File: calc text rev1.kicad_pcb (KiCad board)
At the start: 4 copper layers, 65 x 97.8 mm, 9 parts, among them J1 Conn_ARM_SWD_TagConnect_TC203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

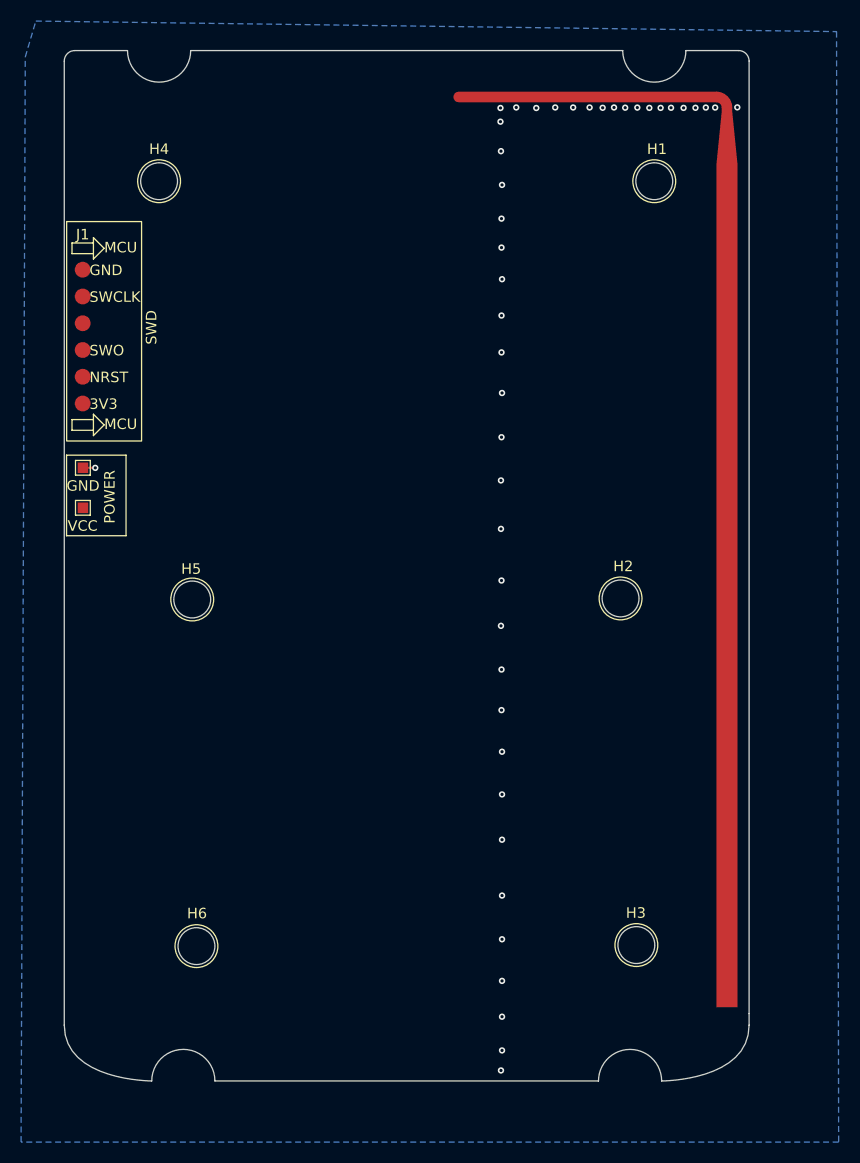
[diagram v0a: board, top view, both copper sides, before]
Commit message: feat: fillet edges + good holes
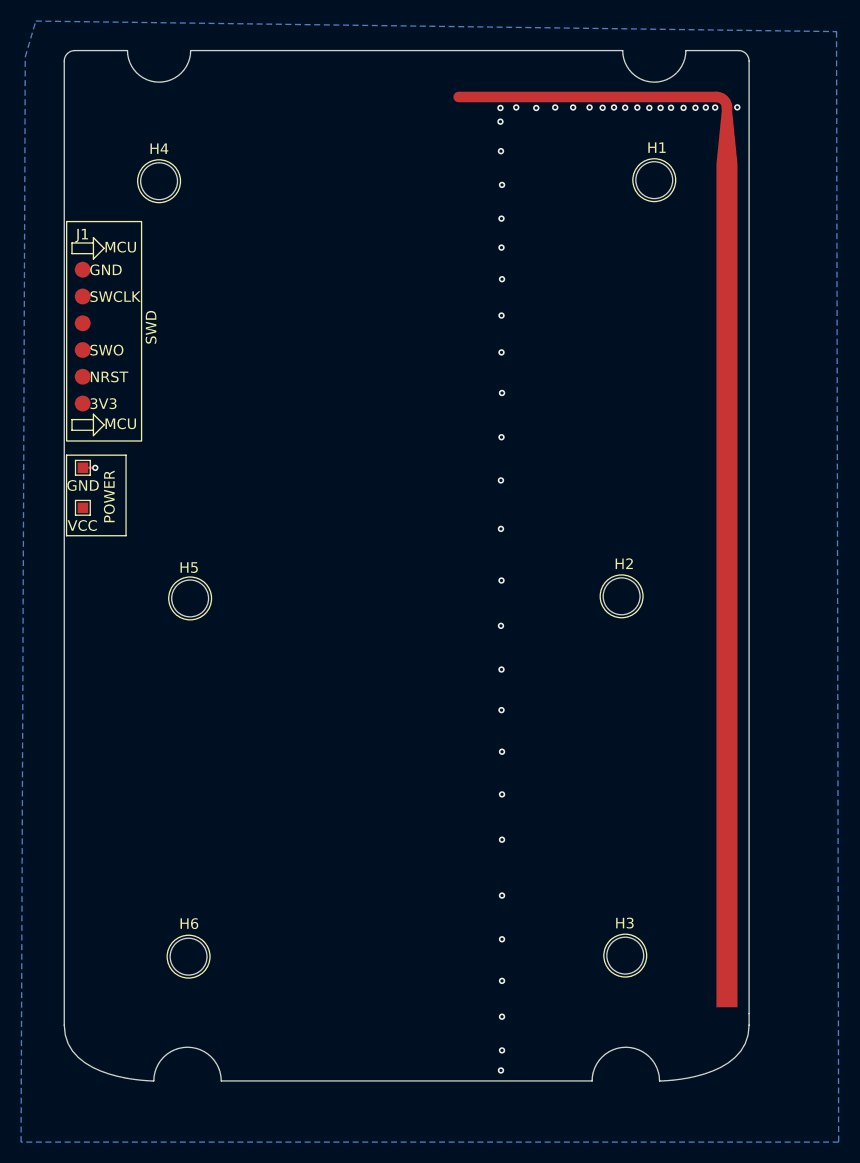
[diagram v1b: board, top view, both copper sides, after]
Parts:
- moved H3 1.45 mm to (70.4, 102.7)
- moved H6 1.25 mm to (29.0, 102.8)
- moved H2 0.22 mm to (70.1, 68.6)
- moved H5 0.22 mm to (29.1, 68.8)
- moved H1 0.10 mm to (73.2, 29.1)
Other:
- outline, holes or cut-outs redrawn
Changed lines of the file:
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@@
 	(footprint "MountingHole:MountingHole_3.5mm_CustomFilled"
 		(layer "F.Cu")
-		(at 69.954 68.8)
+		(at 70.054 68.6)
 		(descr "Mounting Hole 2.1mm, no annular, generated by kicad-footprint-generator mountinghole.py")
 		(tags "mountinghole")
@@
 	(footprint "MountingHole:MountingHole_3.5mm_CustomFilled"
 		(layer "F.Cu")
-		(at 73.154 29.2)
+		(at 73.154 29.1)
 		(descr "Mounting Hole 2.1mm, no annular, generated by kicad-footprint-generator mountinghole.py")
 		(tags "mountinghole")
@@
 	(footprint "MountingHole:MountingHole_3.5mm_CustomFilled"
 		(layer "F.Cu")
-		(at 71.454 101.7)
+		(at 70.4 102.7)
 		(descr "Mounting Hole 2.1mm, no annular, generated by kicad-footprint-generator mountinghole.py")
 		(tags "mountinghole")
@@
 	(footprint "MountingHole:MountingHole_3.5mm_CustomFilled"
 		(layer "F.Cu")
-		(at 29.3 68.9)
+		(at 29.1 68.8)
 		(descr "Mounting Hole 2.1mm, no annular, generated by kicad-footprint-generator mountinghole.py")
 		(tags "mountinghole")
@@
 	(footprint "MountingHole:MountingHole_3.5mm_CustomFilled"
 		(layer "F.Cu")
-		(at 29.7 101.8)
+		(at 28.954 102.8)
 		(descr "Mounting Hole 2.1mm, no annular, generated by kicad-footprint-generator mountinghole.py")
 		(tags "mountinghole")
@@
 		(layer "Edge.Cuts")
 	)
-	(gr_arc
-		(start 25.202538 114.597462)
-		(mid 28.2 111.6)
-		(end 31.197462 114.597462)
-		(stroke
-			(width 0.0381)
-			(type default)
-		)
-		(layer "Edge.Cuts")
-	)
 	(gr_line
 		(start 16.9 17.8)
 		(end 16.9 109.3)
+		(stroke
+			(width 0.0381)
+			(type default)
+		)
+		(layer "Edge.Cuts")
+	)
+	(gr_arc
+		(start 16.9 17.8)
+		(mid 17.192893 17.092893)
+		(end 17.9 16.8)
+		(stroke
+			(width 0.0381)
+			(type default)
+		)
+		(layer "Edge.Cuts")
+	)
+	(gr_arc
+		(start 25.4 114.597462)
+		(mid 28.6 111.397462)
+		(end 31.8 114.597462)
 		(stroke
 			(width 0.0381)
@@
 		(layer "Edge.Cuts")
 	)
-	(gr_line
-		(start 67.605076 114.6)
-		(end 31.197462 114.597462)
-		(stroke
-			(width 0.0381)
-			(type default)
-		)
-		(layer "Edge.Cuts")
-	)
 	(gr_arc
 		(start 28.897462 16.8)
@@
 	)
 	(gr_arc
-		(start 67.605076 114.6)
-		(mid 70.602538 111.602538)
-		(end 73.6 114.6)
-		(stroke
-			(width 0.0381)
-			(type default)
-		)
-		(layer "Edge.Cuts")
-	)
-	(gr_arc
-		(start 16.9 17.8)
-		(mid 17.192893 17.092893)
-		(end 17.9 16.8)
+		(start 80.9 16.8)
+		(mid 81.607107 17.092893)
+		(end 81.9 17.8)
 		(stroke
 			(width 0.0381)
@@
 	(gr_curve
 		(pts
-			(xy 16.9 109.3) (xy 16.9 114.6) (xy 25.202538 114.597462) (xy 25.202538 114.597462)
-		)
+			(xy 16.9 109.3) (xy 16.9 114.6) (xy 25.4 114.597462) (xy 25.4 114.597462)
+		)
+		(stroke
+			(width 0.0381)
+			(type default)
+		)
+		(layer "Edge.Cuts")
+	)
+	(gr_arc
+		(start 67 114.6)
+		(mid 70.2 111.4)
+		(end 73.4 114.6)
+		(stroke
+			(width 0.0381)
+			(type default)
+		)
+		(layer "Edge.Cuts")
+	)
+	(gr_line
+		(start 67 114.6)
+		(end 31.8 114.597462)
 		(stroke
 			(width 0.0381)
@@
 	(gr_curve
 		(pts
-			(xy 81.9 109.3) (xy 81.9 114.6) (xy 73.6 114.6) (xy 73.6 114.6)
-		)
-		(stroke
-			(width 0.0381)
-			(type default)
-		)
-		(layer "Edge.Cuts")
-	)
-	(gr_arc
-		(start 80.9 16.8)
-		(mid 81.607107 17.092893)
-		(end 81.9 17.8)
+			(xy 81.9 109.3) (xy 81.9 114.6) (xy 73.4 114.6) (xy 73.4 114.6)
+		)
 		(stroke
 			(width 0.0381)
@@
 		)
 	)
+	(dimension
+		(type orthogonal)
+		(layer "F.Fab")
+		(pts
+			(xy 28.402538 111.397462) (xy 28.402538 104.8)
+		)
+		(height -3.102538)
+		(orientation 1)
+		(format
+			(prefix "")
+			(suffix "")
+			(units 3)
+			(units_format 0)
+			(precision 4)
+			(suppress_zeroes yes)
+		)
+		(style
+			(thickness 0.1)
+			(arrow_length 1.27)
+			(text_position_mode 0)
+			(arrow_direction outward)
+			(extension_height 0.58642)
+			(extension_offset 0.5)
+			(keep_text_aligned yes)
+		)
+		(gr_text "6.5975"
+			(at 24.15 108.098731 90)
+			(layer "F.Fab")
+			(effects
+				(font
+					(size 1 1)
+					(thickness 0.15)
+				)
+			)
+		)
+	)
+	(dimension
+		(type orthogonal)
+		(layer "F.Fab")
+		(pts
+			(xy 70.4 111.4) (xy 70.4 104.8)
+		)
+		(height 2.7)
+		(orientation 1)
+		(format
+			(prefix "")
+			(suffix "")
+			(units 3)
+			(units_format 0)
+			(precision 4)
+			(suppress_zeroes yes)
+		)
+		(style
+			(thickness 0.1)
+			(arrow_length 1.27)
+			(text_position_mode 0)
+			(arrow_direction outward)
+			(extension_height 0.58642)
+			(extension_offset 0.5)
+			(keep_text_aligned yes)
+		)
+		(gr_text "6.6"
+			(at 71.95 108.1 90)
+			(layer "F.Fab")
+			(effects
+				(font
+					(size 1 1)
+					(thickness 0.15)
+				)
+			)
+		)
+	)

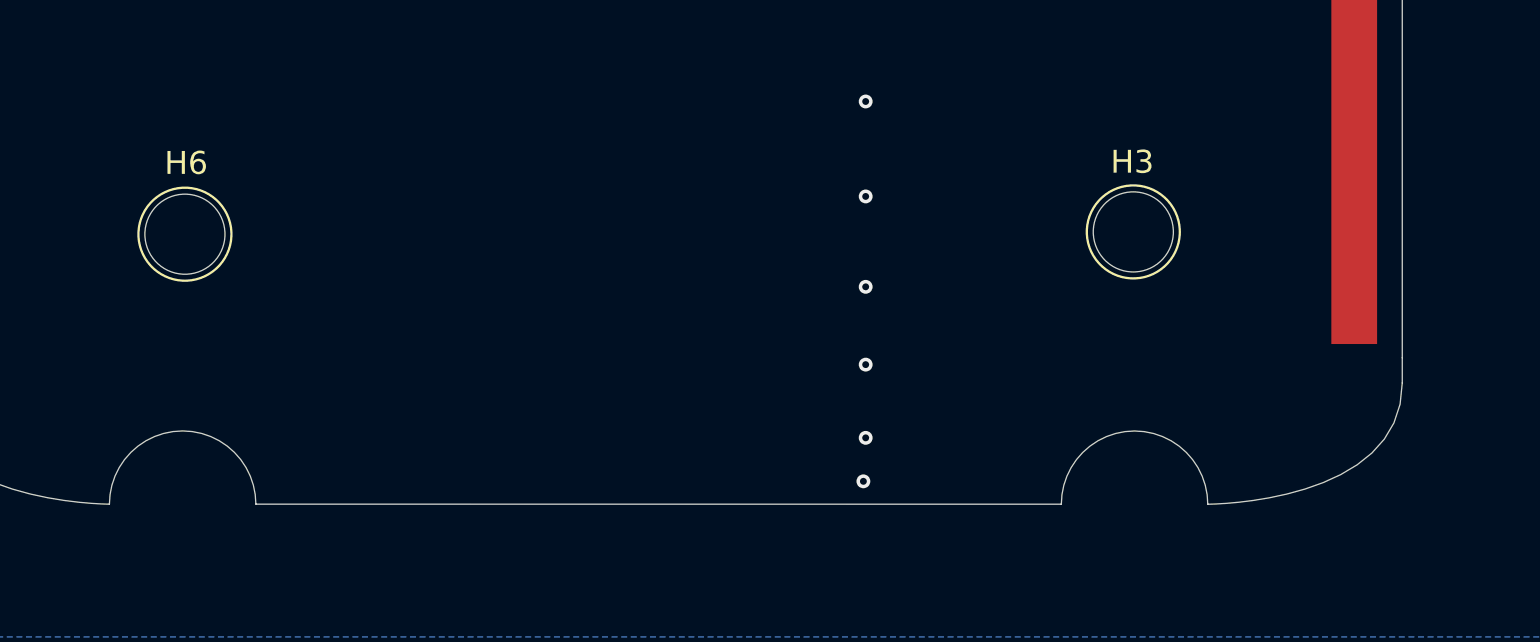
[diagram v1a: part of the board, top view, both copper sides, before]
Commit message: fix: adjust bottom two holes
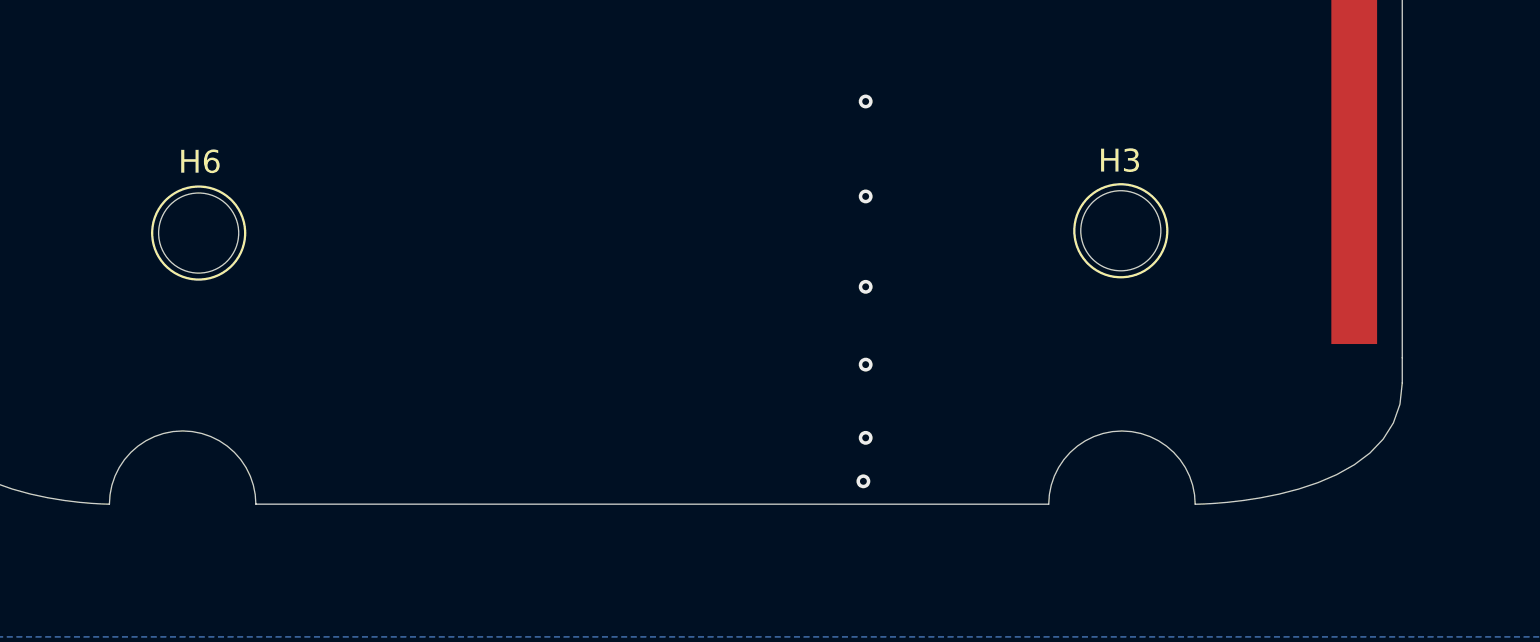
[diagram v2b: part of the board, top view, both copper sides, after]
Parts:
- moved H6 0.60 mm to (29.6, 102.8)
- moved H3 0.55 mm to (69.9, 102.7)
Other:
- outline, holes or cut-outs redrawn
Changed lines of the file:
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@@
 			(outputformat 3)
 			(mirror no)
-			(drillshape 2)
+			(drillshape 1)
 			(scaleselection 1)
 			(outputdirectory "dxf/")
@@
 	(footprint "MountingHole:MountingHole_3.5mm_CustomFilled"
 		(layer "F.Cu")
-		(at 70.4 102.7)
+		(at 69.854 102.65)
 		(descr "Mounting Hole 2.1mm, no annular, generated by kicad-footprint-generator mountinghole.py")
 		(tags "mountinghole")
@@
 	(footprint "MountingHole:MountingHole_3.5mm_CustomFilled"
 		(layer "F.Cu")
-		(at 28.954 102.8)
+		(at 29.554 102.75)
 		(descr "Mounting Hole 2.1mm, no annular, generated by kicad-footprint-generator mountinghole.py")
 		(tags "mountinghole")
@@
 		(layer "Edge.Cuts")
 	)
+	(gr_curve
+		(pts
+			(xy 81.9 109.3) (xy 81.9 114.6) (xy 72.85 114.6) (xy 72.85 114.6)
+		)
+		(stroke
+			(width 0.0381)
+			(type default)
+		)
+		(layer "Edge.Cuts")
+	)
 	(gr_line
 		(start 16.9 17.8)
@@
 		(layer "Edge.Cuts")
 	)
+	(gr_line
+		(start 66.45 114.6)
+		(end 31.8 114.597462)
+		(stroke
+			(width 0.0381)
+			(type default)
+		)
+		(layer "Edge.Cuts")
+	)
 	(gr_arc
 		(start 25.4 114.597462)
@@
 	)
 	(gr_arc
-		(start 67 114.6)
-		(mid 70.2 111.4)
-		(end 73.4 114.6)
-		(stroke
-			(width 0.0381)
-			(type default)
-		)
-		(layer "Edge.Cuts")
-	)
-	(gr_line
-		(start 67 114.6)
-		(end 31.8 114.597462)
-		(stroke
-			(width 0.0381)
-			(type default)
-		)
-		(layer "Edge.Cuts")
-	)
-	(gr_curve
-		(pts
-			(xy 81.9 109.3) (xy 81.9 114.6) (xy 73.4 114.6) (xy 73.4 114.6)
-		)
+		(start 66.45 114.6)
+		(mid 69.65 111.4)
+		(end 72.85 114.6)
 		(stroke
 			(width 0.0381)
@@
 		(layer "F.Fab")
 		(pts
+			(xy 16.9 104.15) (xy 29.2 104)
+		)
+		(height -6.95)
+		(orientation 0)
+		(format
+			(prefix "")
+			(suffix "")
+			(units 3)
+			(units_format 0)
+			(precision 4)
+			(suppress_zeroes yes)
+		)
+		(style
+			(thickness 0.1)
+			(arrow_length 1.27)
+			(text_position_mode 0)
+			(arrow_direction outward)
+			(extension_height 0.58642)
+			(extension_offset 0.5)
+			(keep_text_aligned yes)
+		)
+		(gr_text "12.3"
+			(at 23.05 96.05 0)
+			(layer "F.Fab")
+			(effects
+				(font
+					(size 1 1)
+					(thickness 0.15)
+				)
+			)
+		)
+	)
+	(dimension
+		(type orthogonal)
+		(layer "F.Fab")
+		(pts
 			(xy 70.4 111.4) (xy 70.4 104.8)
 		)
@@
 			(layer "F.Fab")
 			(effects
+				(font
+					(size 1 1)
+					(thickness 0.15)
+				)
+			)
+		)
+	)
+	(dimension
+		(type orthogonal)
+		(layer "F.Fab")
+		(pts
+			(xy 81.9 102.15) (xy 69.6 101.9)
+		)
+		(height -4.5)
+		(orientation 0)
+		(format
+			(prefix "")
+			(suffix "")
+			(units 3)
+			(units_format 0)
+			(precision 4)
+			(suppress_zeroes yes)
+		)
+		(style
+			(thickness 0.1)
+			(arrow_length 1.27)
+			(text_position_mode 0)
+			(arrow_direction outward)
+			(extension_height 0.58642)
+			(extension_offset 0.5)
+			(keep_text_aligned yes)
+		)
+		(gr_text "12.3"
+			(at 75.75 96.5 0)
+			(layer "F.Fab")
+			(effects

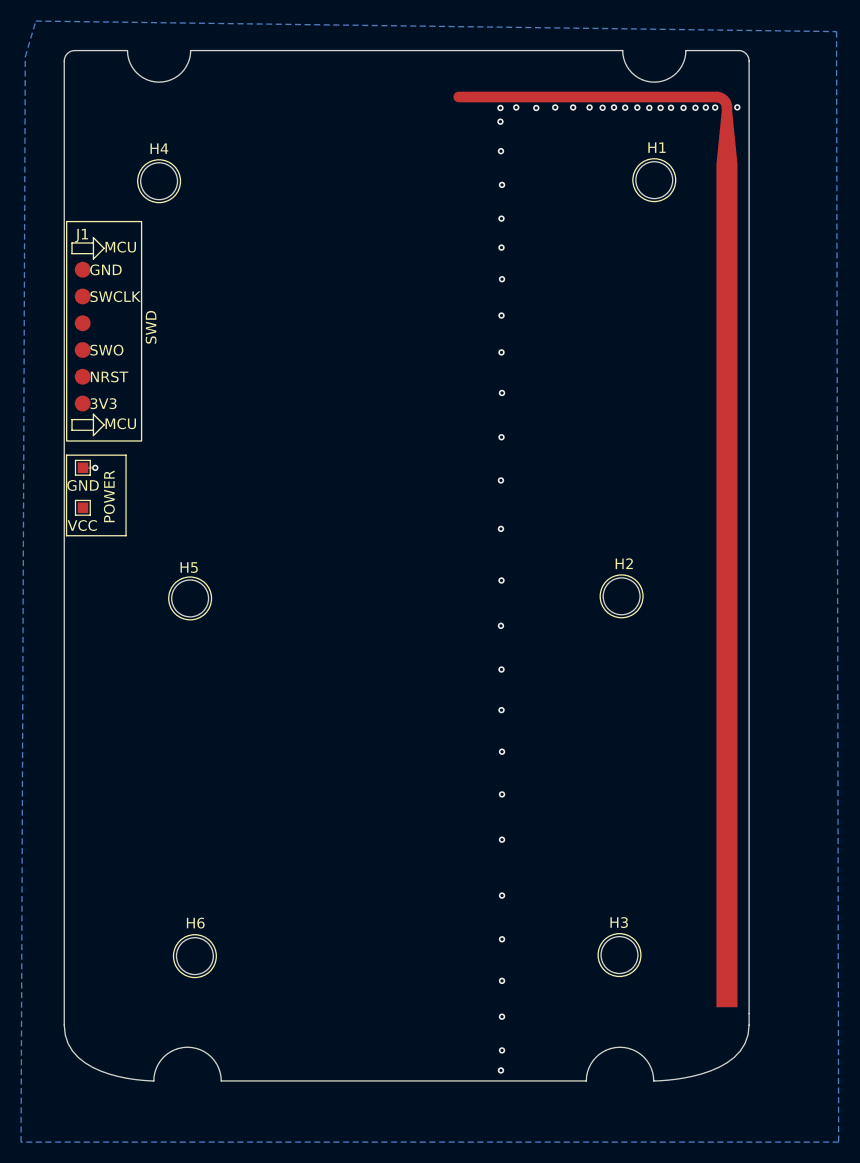
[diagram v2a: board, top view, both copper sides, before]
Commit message: refactor: set hole size to 4.3mm
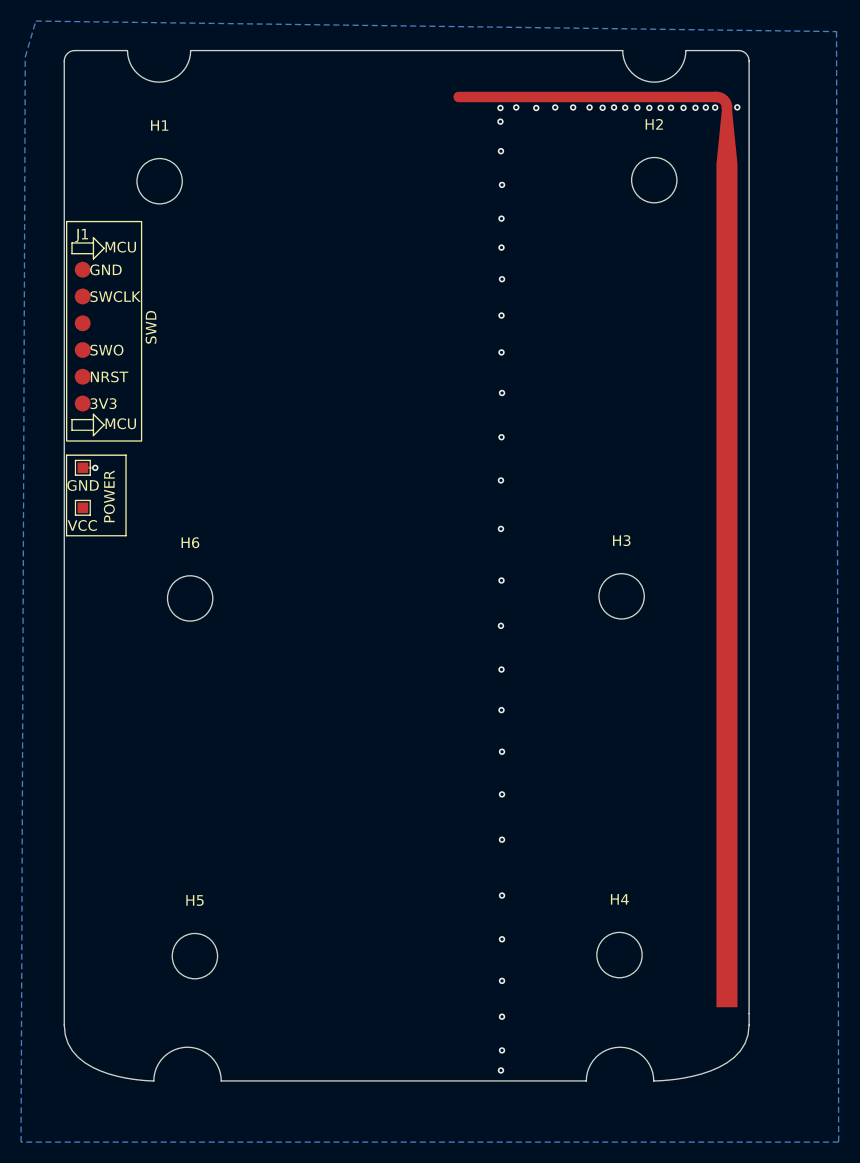
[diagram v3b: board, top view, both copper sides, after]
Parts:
- H1, H2, H3, H4, H5, H6: footprint MountingHole:MountingHole_3.5mm_CustomFilled -> MountingHole:MountingHole_4.3mm_M4
- moved H4 85.3 mm to (69.6, 102.7)
- moved H1 47.2 mm to (25.9, 29.2)
- moved H2 39.6 mm to (72.9, 29.1)
- moved H3 34.1 mm to (69.8, 68.6)
- moved H6 34.0 mm to (28.9, 68.8)
- moved H5 34.0 mm to (29.3, 102.8)
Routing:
- net Net-(AE1-A): track 26.3 -> 0.00 mm
- net (no net): track 0.00 -> 26.3 mm
